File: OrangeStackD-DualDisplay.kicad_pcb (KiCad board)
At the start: 2 copper layers, 48.1 x 46.1 mm, 13 parts, among them J1 DISPLAY, J2 OrangePi, J3 DVMega, J4 GS3, J5 GS3, J6 PWR

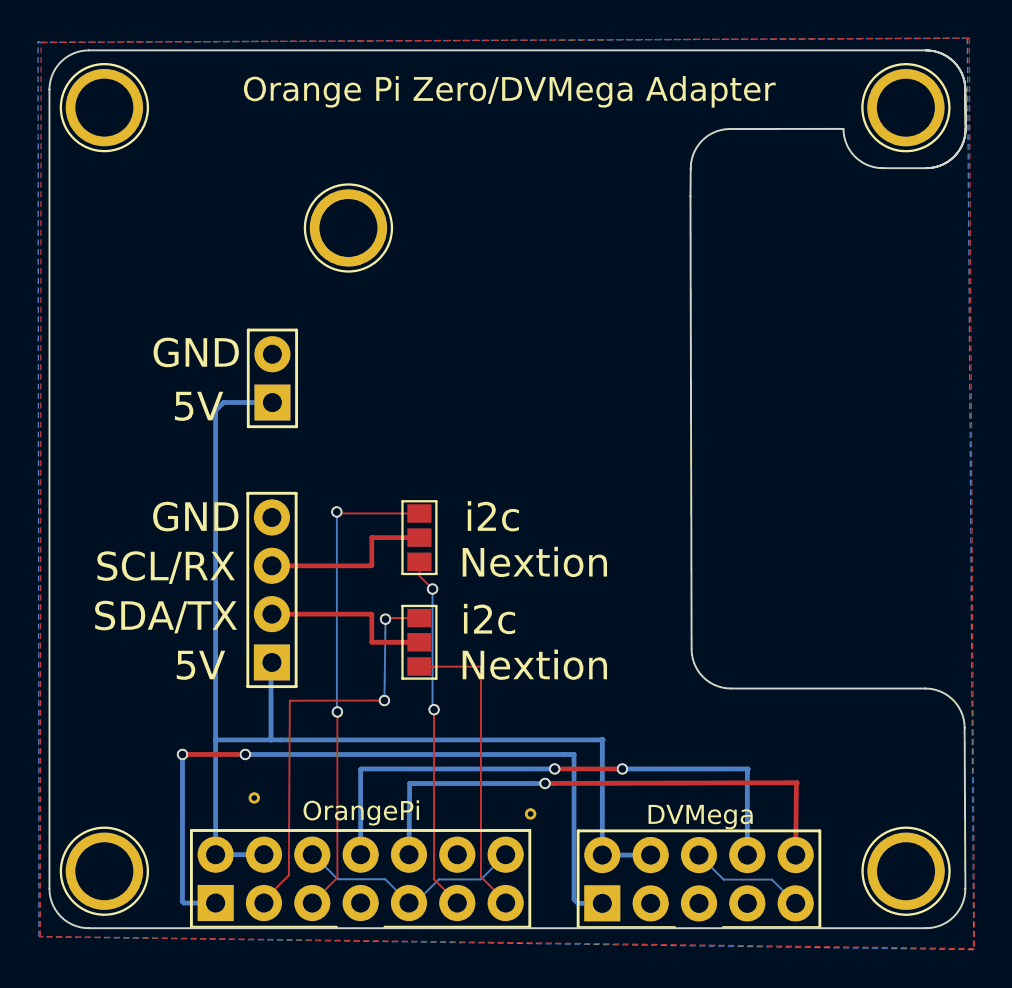
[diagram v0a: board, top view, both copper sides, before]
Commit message: Fixes issue with DVMega connector, adds power filtering and safety features
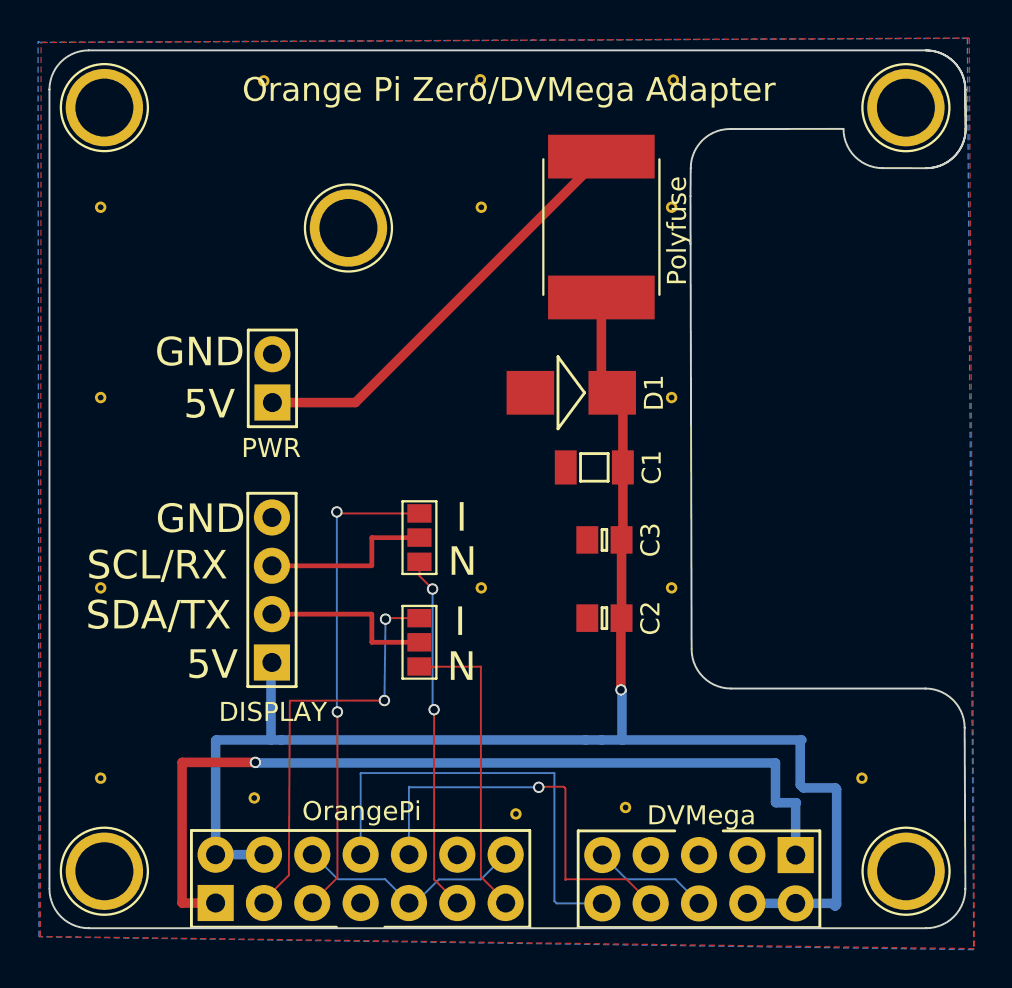
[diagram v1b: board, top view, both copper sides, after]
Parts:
- added C1: 220uF, agg:1206, F.Cu at (166.4, 96.9)
- added C2: 100nF, agg:0805, F.Cu at (166.9, 104.8)
- added C3: 1nF, agg:0805, F.Cu at (166.9, 100.7)
- added D1: ESD_DIODE, agg:DO-214AA-SMB, F.Cu at (165.2, 93.0)
- added F1: Polyfuse, Fuse_Holders_and_Fuses:Fuse_SMD2920, F.Cu at (166.8, 84.3)
- added REF**: VIA-0.6mm, agg:VIA-0.6mm, F.Cu at (180.5, 113.3)
- added REF**: VIA-0.6mm, agg:VIA-0.6mm, F.Cu at (170.5, 93.3)
- added REF**: VIA-0.6mm, agg:VIA-0.6mm, F.Cu at (160.5, 93.3)
- added REF**: VIA-0.6mm, agg:VIA-0.6mm, F.Cu at (150.5, 93.3)
- added REF**: VIA-0.6mm, agg:VIA-0.6mm, F.Cu at (140.5, 93.3)
- added REF**: VIA-0.6mm, agg:VIA-0.6mm, F.Cu at (170.5, 83.3)
- added REF**: VIA-0.6mm, agg:VIA-0.6mm, F.Cu at (160.5, 83.3)
- added REF**: VIA-0.6mm, agg:VIA-0.6mm, F.Cu at (150.5, 83.3)
- added REF**: VIA-0.6mm, agg:VIA-0.6mm, F.Cu at (170.5, 113.3)
- added REF**: VIA-0.6mm, agg:VIA-0.6mm, F.Cu at (168.1, 114.8)
- added REF**: VIA-0.6mm, agg:VIA-0.6mm, F.Cu at (182.7, 113.8)
- added REF**: VIA-0.6mm, agg:VIA-0.6mm, F.Cu at (140.5, 83.3)
- added REF**: VIA-0.6mm, agg:VIA-0.6mm, F.Cu at (160.4, 76.6)
- added REF**: VIA-0.6mm, agg:VIA-0.6mm, F.Cu at (170.6, 76.6)
- added REF**: VIA-0.6mm, agg:VIA-0.6mm, F.Cu at (149.1, 76.6)
- added REF**: VIA-0.6mm, agg:VIA-0.6mm, F.Cu at (160.5, 113.3)
- added REF**: VIA-0.6mm, agg:VIA-0.6mm, F.Cu at (150.5, 113.3)
- added REF**: VIA-0.6mm, agg:VIA-0.6mm, F.Cu at (140.5, 113.3)
- added REF**: VIA-0.6mm, agg:VIA-0.6mm, F.Cu at (170.5, 103.3)
- added REF**: VIA-0.6mm, agg:VIA-0.6mm, F.Cu at (160.5, 103.3)
- added REF**: VIA-0.6mm, agg:VIA-0.6mm, F.Cu at (150.5, 103.3)
- added REF**: VIA-0.6mm, agg:VIA-0.6mm, F.Cu at (140.5, 103.3)
- moved REF** 0.77 mm to (162.3, 115.1)
- turned J3 to 180 degrees
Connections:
- J3 pad 10: /UART1_RX -> /UART1_TX
- J3 pad 8: /UART1_TX -> /UART1_RX
- J6 pad 1: 5v -> Net-(F1-Pad2)
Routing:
- net 5v: track 62.2 -> 85.0 mm, vias 0 -> 1
- net Net-(F1-Pad2): track 0.00 -> 22.6 mm
- net 3v3: track 39.3 -> 46.3 mm, vias 2 -> 1
- net /UART1_RX: track 27.9 -> 21.7 mm
- net /UART1_TX: track 29.4 -> 23.8 mm, vias 2 -> 0
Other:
- net class Biggest added: clearance 0.2, trace_width 0.5, via_dia 0.6, via_drill 0.4
- board text added: "Designed by 2E0SIP (Rev 2) CC BY-NC-SA 4.0 http://2e0sip.co.uk/eam"
- board text added: "I"
- board text added: "N"
- board text added: "Thanks to: G4KLX, PE1PLM & MW0MWZ"
- board text removed: "Designed by 2E0SIP CC BY-NC-SA 4.0 http://2e0sip.co.uk/eam"
- board text removed: "Nextion"
- board text removed: "Thanks to: G4KLX, PE1PLM"
- board text removed: "i2c"

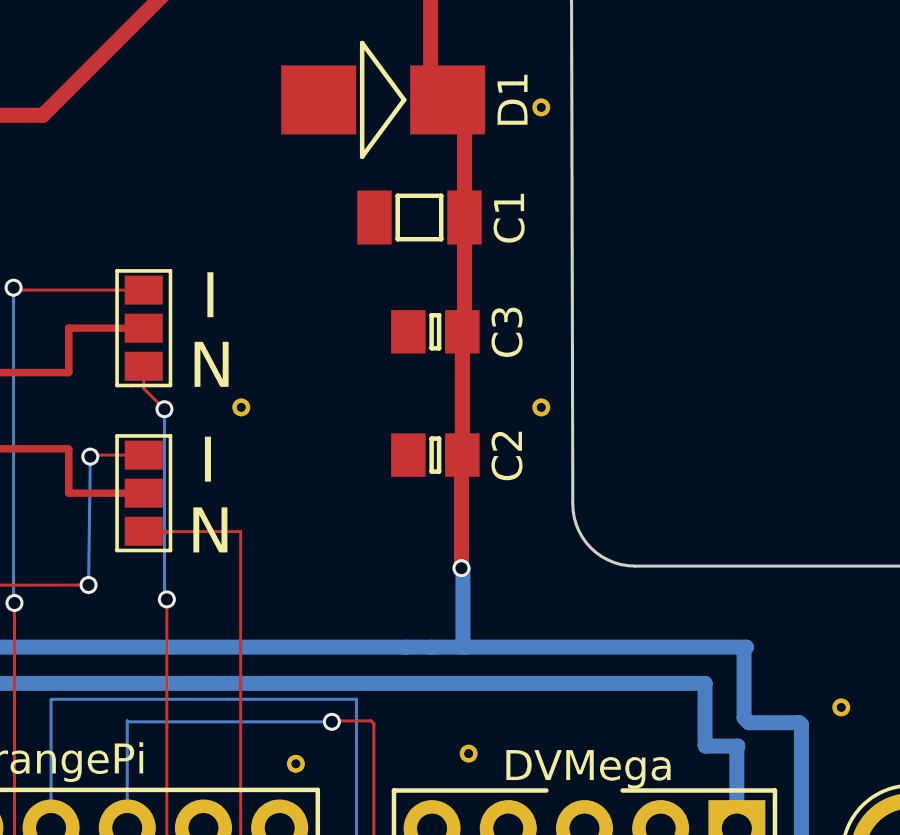
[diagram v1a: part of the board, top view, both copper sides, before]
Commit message: Moves capacitors into correct order
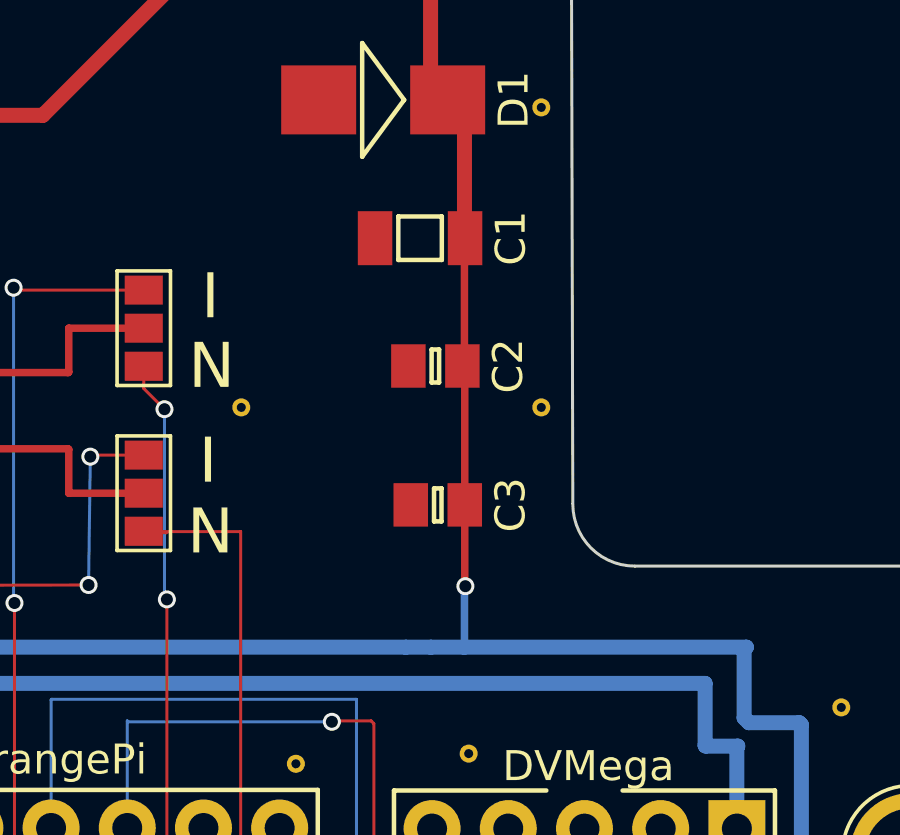
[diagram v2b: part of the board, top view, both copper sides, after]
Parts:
- moved C3 5.77 mm to (167.0, 106.5)
- moved C2 2.97 mm to (166.9, 101.9)
- moved C1 0.69 mm to (166.4, 97.6)
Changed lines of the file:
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@@
     (thickness 1.6)
     (drawings 145)
-    (tracks 133)
+    (tracks 132)
     (zones 0)
     (modules 40)
@@
   (layers
     (0 F.Cu signal)
-    (31 B.Cu signal)
+    (31 B.Cu signal hide)
     (32 B.Adhes user)
     (33 F.Adhes user)
@@
   )
   (module agg:1206 (layer F.Cu)
-    (at 166.42 96.93 180)
+    (at 166.44 97.62 180)
     (fp_text reference C1 (at -3.025 0 270) (layer F.SilkS)
       (effects (font (size 1 1) (thickness 0.15)))
@@
   )
   (module agg:0805 (layer F.Cu)
-    (at 166.95 104.85 180)
+    (at 166.95 101.88 180)
     (fp_text reference C2 (at -2.425 0 270) (layer F.SilkS)
       (effects (font (size 1 1) (thickness 0.15)))
@@
   )
   (module agg:0805 (layer F.Cu)
-    (at 166.95 100.74 180)
+    (at 167.03 106.51 180)
     (fp_text reference C3 (at -2.425 0 270) (layer F.SilkS)
       (effects (font (size 1 1) (thickness 0.15)))
@@
   (gr_circle (center 179.36149 111.685242) (end 180.061488 111.685242) (layer Dwgs.User) (width 0.1))
   (segment (start 157.25 104.88) (end 157.29 104.92) (width 0.2) (layer B.Cu) (net 0))
-  (segment (start 167.85 100.74) (end 167.85 104.85) (width 0.5) (layer F.Cu) (net 1))
-  (segment (start 167.85 104.85) (end 167.82 104.88) (width 0.5) (layer F.Cu) (net 1))
-  (segment (start 167.82 104.88) (end 167.82 108.62) (width 0.5) (layer F.Cu) (net 1))
-  (via (at 167.82 108.62) (size 0.6) (drill 0.4) (layers F.Cu B.Cu) (net 1))
-  (segment (start 167.82 108.62) (end 167.87 108.67) (width 0.5) (layer B.Cu) (net 1))
-  (segment (start 167.87 108.67) (end 167.87 111.212) (width 0.5) (layer B.Cu) (net 1))
-  (segment (start 167.87 111.212) (end 167.91 111.252) (width 0.5) (layer B.Cu) (net 1))
-  (segment (start 167.92 96.93) (end 167.92 100.67) (width 0.5) (layer F.Cu) (net 1))
-  (segment (start 167.92 100.67) (end 167.85 100.74) (width 0.5) (layer F.Cu) (net 1))
+  (segment (start 167.93 106.51) (end 167.93 109.2) (width 0.25) (layer F.Cu) (net 1))
+  (segment (start 167.92 111.242) (end 167.91 111.252) (width 0.25) (layer B.Cu) (net 1))
+  (segment (start 167.92 109.25) (end 167.92 111.242) (width 0.25) (layer B.Cu) (net 1))
+  (segment (start 167.95 109.22) (end 167.92 109.25) (width 0.25) (layer B.Cu) (net 1))
+  (via (at 167.95 109.22) (size 0.6) (drill 0.4) (layers F.Cu B.Cu) (net 1))
+  (segment (start 167.93 109.2) (end 167.95 109.22) (width 0.25) (layer F.Cu) (net 1))
+  (segment (start 167.92 96.93) (end 167.92 101.81) (width 0.25) (layer F.Cu) (net 1))
+  (segment (start 167.92 101.81) (end 167.93 101.82) (width 0.25) (layer F.Cu) (net 1))
+  (segment (start 167.93 101.82) (end 167.93 106.51) (width 0.25) (layer F.Cu) (net 1))
   (segment (start 167.92 96.93) (end 167.92 93.57) (width 0.5) (layer F.Cu) (net 1))
   (segment (start 167.92 93.57) (end 167.36 93.01) (width 0.5) (layer F.Cu) (net 1))
@@
   (segment (start 167.31 88.52) (end 166.79 88) (width 0.5) (layer F.Cu) (net 1))
   (segment (start 166.79 92.5) (end 167.92 93.63) (width 0.5) (layer F.Cu) (net 1))
-  (segment (start 167.92 100.67) (end 167.85 100.74) (width 0.5) (layer F.Cu) (net 1))
   (segment (start 174.46 119.84) (end 177 119.84) (width 0.5) (layer B.Cu) (net 1))
   (segment (start 177 119.84) (end 178.93 119.84) (width 0.5) (layer B.Cu) (net 1))
+  (segment (start 177.318 111.252) (end 177.24 111.33) (width 0.5) (layer B.Cu) (net 1))
+  (segment (start 177.24 111.33) (end 177.24 113.61) (width 0.5) (layer B.Cu) (net 1))
+  (segment (start 177.24 113.61) (end 177.4 113.77) (width 0.5) (layer B.Cu) (net 1))
+  (segment (start 177.4 113.77) (end 179.08 113.77) (width 0.5) (layer B.Cu) (net 1))
+  (segment (start 179.08 113.77) (end 179.15 113.84) (width 0.5) (layer B.Cu) (net 1))
+  (segment (start 179.15 113.84) (end 179.15 119.9) (width 0.5) (layer B.Cu) (net 1))
+  (segment (start 179.15 119.9) (end 179.07 119.98) (width 0.5) (layer B.Cu) (net 1))
+  (segment (start 177.318 111.252) (end 167.91 111.252) (width 0.5) (layer B.Cu) (net 1))
   (segment (start 178.93 119.84) (end 179.07 119.98) (width 0.5) (layer B.Cu) (net 1))
-  (segment (start 177.318 111.252) (end 167.91 111.252) (width 0.5) (layer B.Cu) (net 1))
   (segment (start 167.91 111.252) (end 166.8 111.252) (width 0.5) (layer B.Cu) (net 1))
-  (segment (start 179.15 119.9) (end 179.07 119.98) (width 0.5) (layer B.Cu) (net 1))
-  (segment (start 179.15 113.84) (end 179.15 119.9) (width 0.5) (layer B.Cu) (net 1))
-  (segment (start 179.08 113.77) (end 179.15 113.84) (width 0.5) (layer B.Cu) (net 1))
-  (segment (start 177.4 113.77) (end 179.08 113.77) (width 0.5) (layer B.Cu) (net 1))
-  (segment (start 177.24 113.61) (end 177.4 113.77) (width 0.5) (layer B.Cu) (net 1))
-  (segment (start 177.24 111.33) (end 177.24 113.61) (width 0.5) (layer B.Cu) (net 1))
-  (segment (start 177.318 111.252) (end 177.24 111.33) (width 0.5) (layer B.Cu) (net 1))
   (segment (start 149.43 111.252) (end 149.43 107.23) (width 0.5) (layer B.Cu) (net 1))
   (segment (start 149.43 107.23) (end 149.48 107.18) (width 0.25) (layer B.Cu) (net 1))

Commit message: Adds power LED
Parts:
- added D2: LED, agg:0805-LED, F.Cu at (184.1, 112.7)
- added R1: 680, agg:0805, F.Cu at (181.5, 112.7)
- moved REF** 1.47 mm to (179.1, 112.8)
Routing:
- net 5v: track 84.9 -> 100.2 mm
- net Net-(D2-Pad2): track 0.00 -> 2.58 mm
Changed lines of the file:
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@@
 (kicad_pcb (version 4) (host pcbnew 4.0.6)
   (general
-    (links 45)
+    (links 48)
     (no_connects 0)
     (area 137.738695 74.966545 185.981305 121.193455)
     (thickness 1.6)
     (drawings 145)
-    (tracks 132)
+    (tracks 137)
     (zones 0)
-    (modules 40)
-    (nets 18)
+    (modules 42)
+    (nets 19)
   )
   (page A4)
   (layers
     (0 F.Cu signal)
-    (31 B.Cu signal hide)
+    (31 B.Cu signal)
     (32 B.Adhes user)
     (33 F.Adhes user)
@@
     (mod_text_size 1 1)
     (mod_text_width 0.15)
-    (pad_size 0.6 0.6)
-    (pad_drill 0.3)
+    (pad_size 1.15 1.45)
+    (pad_drill 0)
     (pad_to_mask_clearance 0.2)
     (aux_axis_origin 137.62 75.3)
@@
   (net 16 "Net-(J3-Pad7)")
   (net 17 "Net-(F1-Pad2)")
+  (net 18 "Net-(D2-Pad2)")
   (net_class Default "This is the default net class."
     (clearance 0.2)
@@
     (add_net 5v)
     (add_net GND)
+    (add_net "Net-(D2-Pad2)")
     (add_net "Net-(F1-Pad2)")
     (add_net "Net-(J2-Pad12)")
@@
   )
   (module agg:VIA-0.6mm (layer F.Cu)
-    (at 180.48 113.26)
+    (at 179.1 112.76)
     (fp_text reference REF** (at 0 1.27) (layer F.SilkS) hide
       (effects (font (size 1 1) (thickness 0.15)))
@@
     (pad 1 thru_hole circle (at 0 0) (size 0.6 0.6) (drill 0.3) (layers *.Cu)
       (net 4 GND) (zone_connect 2))
+  )
+  (module agg:0805-LED (layer F.Cu)
+    (at 184.08 112.66 90)
+    (fp_text reference D2 (at 2.44 -0.45 180) (layer F.SilkS)
+      (effects (font (size 1 1) (thickness 0.15)))
+    )
+    (fp_text value LED (at -2.51 0.3 180) (layer F.Fab)
+      (effects (font (size 1 1) (thickness 0.15)))
+    )
+    (fp_line (start -1 -0.625) (end 1 -0.625) (layer F.Fab) (width 0.01))
+    (fp_line (start 1 -0.625) (end 1 0.625) (layer F.Fab) (width 0.01))
+    (fp_line (start 1 0.625) (end -1 0.625) (layer F.Fab) (width 0.01))
+    (fp_line (start -1 0.625) (end -1 -0.625) (layer F.Fab) (width 0.01))
+    (fp_line (start -0.5 -0.625) (end -0.5 0.625) (layer F.Fab) (width 0.01))
+    (fp_line (start -0.5 -0.625) (end -0.5 0.625) (layer F.Fab) (width 0.01))
+    (fp_line (start 0.5 -0.625) (end 0.5 0.625) (layer F.Fab) (width 0.01))
+    (fp_line (start -0.125 0) (end 0.125 -0.55) (layer F.SilkS) (width 0.15))
+    (fp_line (start -0.125 0) (end 0.125 0.55) (layer F.SilkS) (width 0.15))
+    (fp_line (start 0.125 -0.55) (end 0.125 0.55) (layer F.SilkS) (width 0.15))
+    (fp_line (start -1.75 -1) (end 1.75 -1) (layer F.CrtYd) (width 0.01))
+    (fp_line (start 1.75 -1) (end 1.75 1) (layer F.CrtYd) (width 0.01))
+    (fp_line (start 1.75 1) (end -1.75 1) (layer F.CrtYd) (width 0.01))
+    (fp_line (start -1.75 1) (end -1.75 -1) (layer F.CrtYd) (width 0.01))
+    (pad 1 smd rect (at -0.9 0 90) (size 1.15 1.45) (layers F.Cu F.Paste F.Mask)
+      (net 4 GND) (zone_connect 1))
+    (pad 2 smd rect (at 0.9 0 90) (size 1.15 1.45) (layers F.Cu F.Paste F.Mask)
+      (net 18 "Net-(D2-Pad2)"))
+    (model ${KISYS3DMOD}/LEDs.3dshapes/LED_0805.wrl
+      (at (xyz -0.006 0 0))
+      (scale (xyz 1 1 1))
+      (rotate (xyz 0 0 0))
+    )
+  )
+  (module agg:0805 (layer F.Cu)
+    (at 181.5 112.65 90)
+    (fp_text reference R1 (at 2.45 -0.12 180) (layer F.SilkS)
+      (effects (font (size 1 1) (thickness 0.15)))
+    )
+    (fp_text value 680 (at -2.4 0.02 360) (layer F.Fab)
+      (effects (font (size 1 1) (thickness 0.15)))
+    )
+    (fp_line (start -1 -0.625) (end 1 -0.625) (layer F.Fab) (width 0.01))
+    (fp_line (start 1 -0.625) (end 1 0.625) (layer F.Fab) (width 0.01))
+    (fp_line (start 1 0.625) (end -1 0.625) (layer F.Fab) (width 0.01))
+    (fp_line (start -1 0.625) (end -1 -0.625) (layer F.Fab) (width 0.01))
+    (fp_line (start -0.5 -0.625) (end -0.5 0.625) (layer F.Fab) (width 0.01))
+    (fp_line (start 0.5 -0.625) (end 0.5 0.625) (layer F.Fab) (width 0.01))
+    (fp_line (start -0.125 -0.55) (end 0.125 -0.55) (layer F.SilkS) (width 0.15))
+    (fp_line (start 0.125 -0.55) (end 0.125 0.55) (layer F.SilkS) (width 0.15))
+    (fp_line (start 0.125 0.55) (end -0.125 0.55) (layer F.SilkS) (width 0.15))
+    (fp_line (start -0.125 0.55) (end -0.125 -0.55) (layer F.SilkS) (width 0.15))
+    (fp_line (start -1.75 -1) (end 1.75 -1) (layer F.CrtYd) (width 0.01))
+    (fp_line (start 1.75 -1) (end 1.75 1) (layer F.CrtYd) (width 0.01))
+    (fp_line (start 1.75 1) (end -1.75 1) (layer F.CrtYd) (width 0.01))
+    (fp_line (start -1.75 1) (end -1.75 -1) (layer F.CrtYd) (width 0.01))
+    (pad 1 smd rect (at -0.9 0 90) (size 1.15 1.45) (layers F.Cu F.Paste F.Mask)
+      (net 1 5v))
+    (pad 2 smd rect (at 0.9 0 90) (size 1.15 1.45) (layers F.Cu F.Paste F.Mask)
+      (net 18 "Net-(D2-Pad2)"))
+    (model ${KISYS3DMOD}/Resistors_SMD.3dshapes/R_0805.wrl
+      (at (xyz 0 0 0))
+      (scale (xyz 1 1 1))
+      (rotate (xyz 0 0 0))
+    )
   )
   (gr_line (start 188.944706 90.099102) (end 188.944706 106.609102) (layer Dwgs.User) (width 0.1))
@@
   (gr_circle (center 179.36149 111.685242) (end 180.061488 111.685242) (layer Dwgs.User) (width 0.1))
   (segment (start 157.25 104.88) (end 157.29 104.92) (width 0.2) (layer B.Cu) (net 0))
+  (segment (start 167.95 109.22) (end 168.76 109.22) (width 0.25) (layer F.Cu) (net 1))
+  (segment (start 173.09 113.55) (end 181.5 113.55) (width 0.25) (layer F.Cu) (net 1))
+  (segment (start 168.76 109.22) (end 173.09 113.55) (width 0.25) (layer F.Cu) (net 1))
   (segment (start 167.93 106.51) (end 167.93 109.2) (width 0.25) (layer F.Cu) (net 1))
   (segment (start 167.92 111.242) (end 167.91 111.252) (width 0.25) (layer B.Cu) (net 1))
@@
   (segment (start 149.5044 93.5228) (end 153.8672 93.5228) (width 0.5) (layer F.Cu) (net 17))
   (segment (start 153.8672 93.5228) (end 166.79 80.6) (width 0.5) (layer F.Cu) (net 17))
+  (segment (start 181.5 111.75) (end 184.07 111.75) (width 0.25) (layer F.Cu) (net 18))
+  (segment (start 184.07 111.75) (end 184.08 111.76) (width 0.25) (layer F.Cu) (net 18))
   (zone (net 4) (net_name GND) (layer F.Cu) (hatch edge 0.508)
     (connect_pads thru_hole_only (clearance 0.508))
